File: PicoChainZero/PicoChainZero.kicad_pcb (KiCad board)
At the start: 2 copper layers, 60 x 60 mm, 16 parts, among them J1 RJ45, J2 RJ45, J4 +24V, J5 Conn_02x20_Odd_Even, J6 +12V, J7 USB_C_Receptacle_USB2.0_14P, U1 LM78M05, U2 PCA9615DP, U3 FT232RL

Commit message: Added open source hardware logo to PCBs
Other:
- board text added: "The TAPR Open Hardware License http://www.tapr.org/OHL"

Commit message: Regenerated gerbers
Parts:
- J4: value +24V -> Screw Terminal
- J6: value +12V -> Screw Terminal
- U1: value LM78M05 -> LM78M05_TO252
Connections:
- U3 pad 4: unconnected-(U3-VCCIO-Pad4) -> +5V
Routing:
- net +5V: track 57.9 -> 80.4 mm, vias 0 -> 2

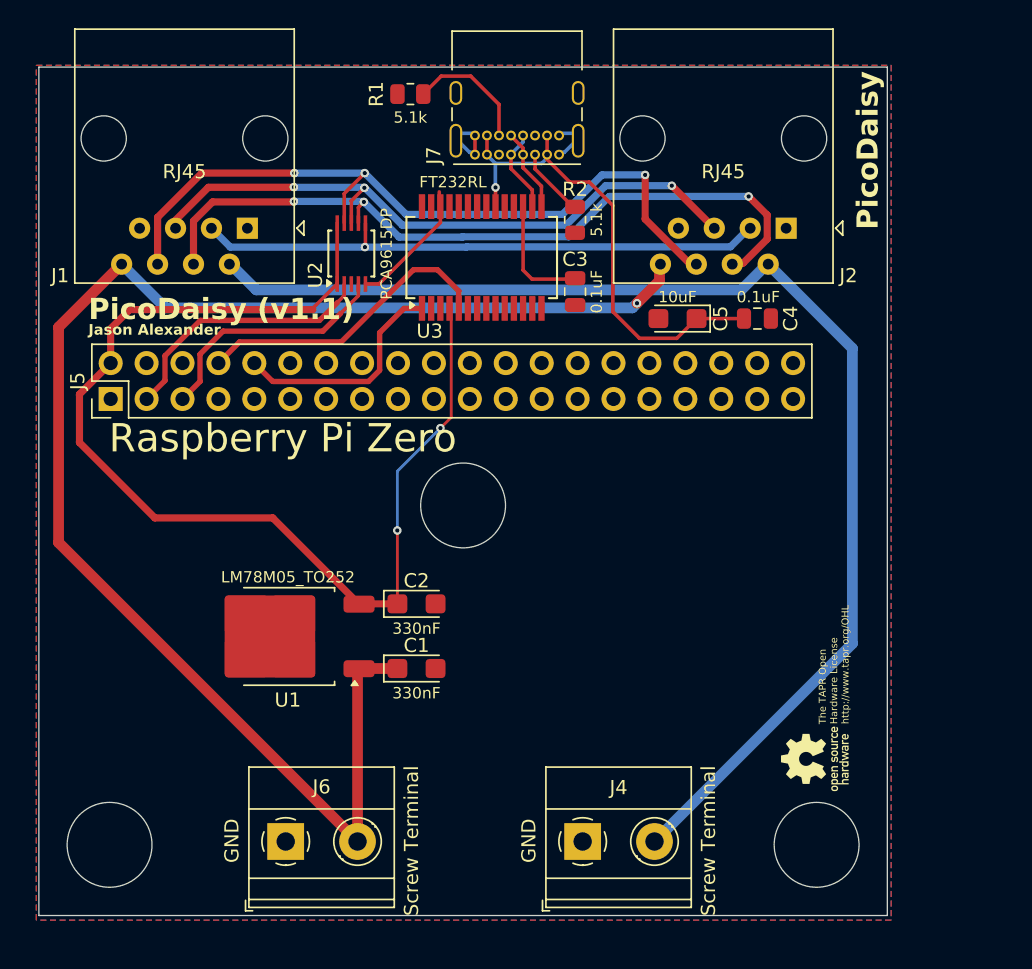
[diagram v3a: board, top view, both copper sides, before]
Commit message: Made pass through power rails larger.
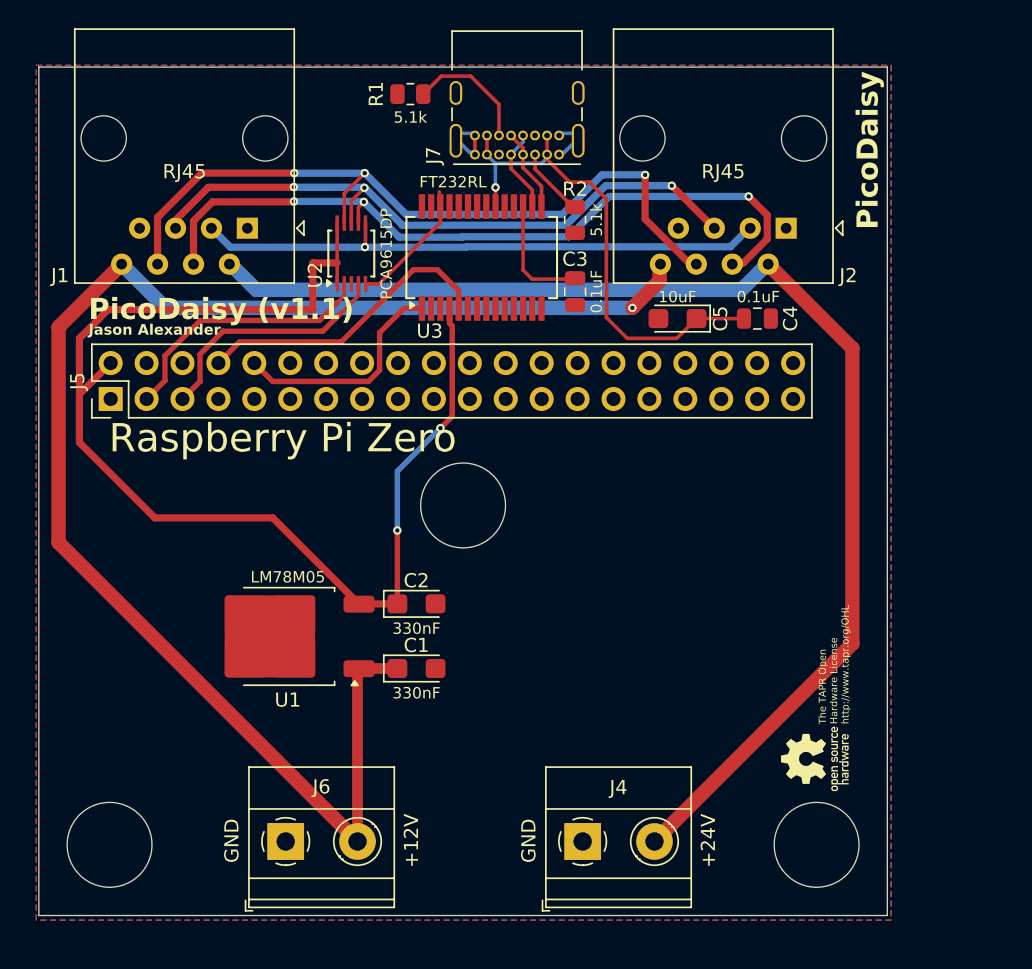
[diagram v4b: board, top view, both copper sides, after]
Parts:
- J4: value Screw Terminal -> +24V
- J6: value Screw Terminal -> +12V
- U1: value LM78M05_TO252 -> LM78M05
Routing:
- net +5V: track 80.4 -> 87.1 mm
- net Net-(U3-VCC): track 35.5 -> 36.0 mm
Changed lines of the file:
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@@
 			)
 		)
-		(property "Value" "Screw Terminal"
+		(property "Value" "+12V"
 			(at 8.895 -0.051 90)
 			(layer "F.SilkS")
@@
 			)
 		)
-		(property "Value" "Screw Terminal"
+		(property "Value" "+24V"
 			(at 8.895 -0.051 90)
 			(layer "F.SilkS")
@@
 		(tags "USB Type-C Receptacle Through-hole Right angle")
 		(property "Reference" "J7"
-			(at 8.865 -0.067 90)
+			(at 8.8746 -0.0644 90)
 			(layer "F.SilkS")
 			(effects
@@
 			)
 		)
-		(property "Value" "LM78M05_TO252"
+		(property "Value" "LM78M05"
 			(at -0.01 4.191 0)
 			(layer "F.SilkS")
@@
 	)
 	(segment
-		(start 105.077 58.499)
-		(end 105.077 60.932)
-		(width 0.508)
+		(start 125.353 72.775)
+		(end 125.353 77.959)
+		(width 0.381)
 		(layer "F.Cu")
 		(net 2)
 	)
 	(segment
-		(start 119.38 57.15)
-		(end 119.38 57.05)
-		(width 0.254)
+		(start 104.902 57.15)
+		(end 119.38 57.15)
+		(width 0.508)
 		(layer "F.Cu")
 		(net 2)
 	)
 	(segment
-		(start 129.159 64.77)
-		(end 128.397 65.532)
+		(start 129.043 57.067)
+		(end 129.159 57.183)
 		(width 0.2)
 		(layer "F.Cu")
@@
 	)
 	(segment
-		(start 125.353 72.775)
-		(end 125.353 77.959)
-		(width 0.2)
+		(start 121.095 53.848)
+		(end 121.095 51.035)
+		(width 0.254)
 		(layer "F.Cu")
 		(net 2)
 	)
 	(segment
-		(start 106.426 57.15)
-		(end 105.077 58.499)
+		(start 102.87 63.139)
+		(end 102.87 59.182)
 		(width 0.508)
 		(layer "F.Cu")
@@
 	)
 	(segment
-		(start 129.043 57.067)
-		(end 129.159 57.183)
-		(width 0.2)
+		(start 102.87 59.182)
+		(end 104.902 57.15)
+		(width 0.508)
+		(layer "F.Cu")
+		(net 2)
+	)
+	(segment
+		(start 129.2352 58.30522)
+		(end 129.043 58.11302)
+		(width 0.381)
 		(layer "F.Cu")
 		(net 2)
@@
 	)
 	(segment
+		(start 129.2352 64.6938)
+		(end 129.2352 58.30522)
+		(width 0.381)
+		(layer "F.Cu")
+		(net 2)
+	)
+	(segment
 		(start 119.38 57.15)
-		(end 106.426 57.15)
+		(end 119.38 53.848)
 		(width 0.508)
 		(layer "F.Cu")
@@
 	)
 	(segment
+		(start 121.095 55.335)
+		(end 121.095 53.848)
+		(width 0.254)
+		(layer "F.Cu")
+		(net 2)
+	)
+	(segment
 		(start 102.87 66.548)
 		(end 108.204 71.882)
@@
 	)
 	(segment
-		(start 129.159 57.183)
-		(end 129.159 64.77)
-		(width 0.2)
+		(start 105.077 60.932)
+		(end 102.87 63.139)
+		(width 0.508)
 		(layer "F.Cu")
 		(net 2)
 	)
 	(segment
-		(start 105.077 60.932)
-		(end 102.87 63.139)
-		(width 0.508)
+		(start 128.397 65.532)
+		(end 129.2352 64.6938)
+		(width 0.381)
 		(layer "F.Cu")
 		(net 2)
@@
 	)
 	(segment
-		(start 121.095 55.335)
-		(end 121.095 51.035)
-		(width 0.254)
+		(start 125.353 77.959)
+		(end 122.667 77.959)
+		(width 0.508)
 		(layer "F.Cu")
 		(net 2)
 	)
 	(segment
-		(start 125.353 77.959)
-		(end 122.667 77.959)
-		(width 0.508)
+		(start 129.043 58.11302)
+		(end 129.043 57.067)
+		(width 0.381)
 		(layer "F.Cu")
 		(net 2)
@@
 	)
 	(segment
-		(start 119.38 57.05)
-		(end 121.095 55.335)
-		(width 0.254)
+		(start 125.353 72.767)
+		(end 125.349 72.771)
+		(width 0.2)
 		(layer "F.Cu")
 		(net 2)
 	)
 	(segment
-		(start 125.353 72.767)
-		(end 125.349 72.771)
-		(width 0.2)
+		(start 119.38 53.848)
+		(end 121.095 53.848)
+		(width 0.508)
 		(layer "F.Cu")
 		(net 2)
@@
 		(start 128.397 65.532)
 		(end 125.353 68.576)
-		(width 0.2)
+		(width 0.381)
 		(layer "B.Cu")
 		(net 2)
@@
 		(start 125.353 68.576)
 		(end 125.353 72.767)
-		(width 0.2)
+		(width 0.381)
 		(layer "B.Cu")
 		(net 2)
@@
 		(start 105.8545 53.936)
 		(end 101.394 58.3965)
-		(width 0.762)
+		(width 1.016)
 		(layer "F.Cu")
 		(net 3)
 	)
 	(segment
-		(start 142.299 56.701)
-		(end 143.891 55.109)
+		(start 125.353 82.531)
+		(end 122.655 82.531)
 		(width 0.762)
 		(layer "F.Cu")
@@
 	)
 	(segment
-		(start 143.891 55.109)
-		(end 143.891 53.9995)
+		(start 122.535 82.651)
+		(end 122.642 82.544)
 		(width 0.762)
 		(layer "F.Cu")
@@
 	)
 	(segment
-		(start 125.353 82.531)
-		(end 122.655 82.531)
-		(width 0.762)
+		(start 143.891 55.109)
+		(end 143.891 53.9995)
+		(width 1.016)
 		(layer "F.Cu")
 		(net 3)
 	)
 	(segment
-		(start 122.535 82.651)
-		(end 122.642 82.544)
+		(start 143.891 53.9995)
+		(end 143.9545 53.936)
 		(width 0.762)
 		(layer "F.Cu")
@@
 	)
 	(segment
-		(start 143.891 53.9995)
-		(end 143.9545 53.936)
-		(width 0.762)
+		(start 141.973 57.027)
+		(end 143.891 55.109)
+		(width 1.016)
 		(layer "F.Cu")
 		(net 3)
@@
 		(start 101.394 73.624)
 		(end 122.535 94.765)
-		(width 0.762)
+		(width 1.016)
 		(layer "F.Cu")
 		(net 3)
@@
 		(start 101.394 58.3965)
 		(end 101.394 73.624)
-		(width 0.762)
+		(width 1.016)
 		(layer "F.Cu")
 		(net 3)
 	)
 	(via
-		(at 142.299 56.701)
+		(at 141.973 57.027)
 		(size 0.6)
 		(drill 0.3)
@@
 	)
 	(segment
-		(start 142.299 56.701)
-		(end 141.973 57.027)
-		(width 0.762)
-		(layer "B.Cu")
-		(net 3)
-	)
-	(segment
 		(start 108.9455 57.027)
 		(end 105.8545 53.936)
-		(width 0.762)
+		(width 1.016)
 		(layer "B.Cu")
 		(net 3)
@@
 		(start 141.973 57.027)
 		(end 108.9455 57.027)
-		(width 0.762)
+		(width 1.016)
 		(layer "B.Cu")
 		(net 3)
@@
 	)
 	(segment
-		(start 137.541 48.133)
-		(end 135.939 46.531)
+		(start 131.689 46.034)
+		(end 131.689 44.684)
 		(width 0.254)
 		(layer "F.Cu")
@@
 	)
 	(segment
-		(start 131.689 46.034)
-		(end 131.689 44.684)
+		(start 138.938 48.133)
+		(end 137.541 48.133)
 		(width 0.254)
 		(layer "F.Cu")
@@
 	)
 	(segment
-		(start 145.114 59.182)
-		(end 142.478 59.182)
+		(start 141.605 59.182)
+		(end 140.1318 57.7088)
 		(width 0.254)
 		(layer "F.Cu")
@@
 	)
 	(segment
-		(start 140.589 57.293)
-		(end 140.589 49.784)
+		(start 137.541 48.133)
+		(end 135.939 46.531)
 		(width 0.254)
 		(layer "F.Cu")
@@
 	)
 	(segment
-		(start 140.589 49.784)
-		(end 138.938 48.133)
+		(start 135.939 46.531)
+		(end 135.939 44.684)
 		(width 0.254)
 		(layer "F.Cu")
@@
 	)
 	(segment
-		(start 138.938 48.133)
-		(end 137.541 48.133)
+		(start 132.293 48.514)
+		(end 132.293 49.867)
 		(width 0.254)
 		(layer "F.Cu")
@@
 	)
 	(segment
-		(start 132.293 48.514)
-		(end 132.293 49.867)
+		(start 140.1318 49.3268)
+		(end 138.938 48.133)
 		(width 0.254)
 		(layer "F.Cu")
@@
 	)
 	(segment
-		(start 142.478 59.182)
-		(end 140.589 57.293)
+		(start 145.114 59.182)
+		(end 141.605 59.182)
 		(width 0.254)
 		(layer "F.Cu")
@@
 	)
 	(segment
-		(start 135.939 46.531)
-		(end 135.939 44.684)
+		(start 146.511 57.785)
+		(end 145.114 59.182)
 		(width 0.254)
 		(layer "F.Cu")
@@
 	)
 	(segment
-		(start 146.511 57.785)
-		(end 145.114 59.182)
+		(start 140.1318 57.7088)
+		(end 140.1318 49.3268)
 		(width 0.254)
 		(layer "F.Cu")
@@
 		(start 157.528 80.772)
 		(end 157.528 59.8895)
-		(width 0.762)
-		(layer "B.Cu")
+		(width 1.016)
+		(layer "F.Cu")
 		(net 11)
 	)
 	(segment
-		(start 113.4745 53.856)
-		(end 115.3755 55.757)
-		(width 0.762)
-		(layer "B.Cu")
+		(start 151.5745 53.936)
+		(end 157.528 59.8895)
+		(width 1.016)
+		(layer "F.Cu")
 		(net 11)
 	)
 	(segment
-		(start 115.3755 55.757)
-		(end 149.6735 55.757)
-		(width 0.762)
-		(layer "B.Cu")
+		(start 143.535 94.765)
+		(end 157.528 80.772)
+		(width 1.016)
+		(layer "F.Cu")
 		(net 11)
 	)
 	(segment
-		(start 151.5745 53.936)
-		(end 157.528 59.8895)
-		(width 0.762)
+		(start 113.4745 53.856)
+		(end 115.3755 55.757)
+		(width 1.016)
 		(layer "B.Cu")
 		(net 11)
 	)
 	(segment
-		(start 143.535 94.765)
-		(end 157.528 80.772)
-		(width 0.762)
+		(start 115.3755 55.757)
+		(end 149.6735 55.757)
+		(width 1.016)
 		(layer "B.Cu")
 		(net 11)
@@
 		(start 149.6735 55.757)
 		(end 151.5745 53.856)
-		(width 0.762)
+		(width 1.016)
 		(layer "B.Cu")
 		(net 11)

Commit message: Updated PicoChainZero base board.
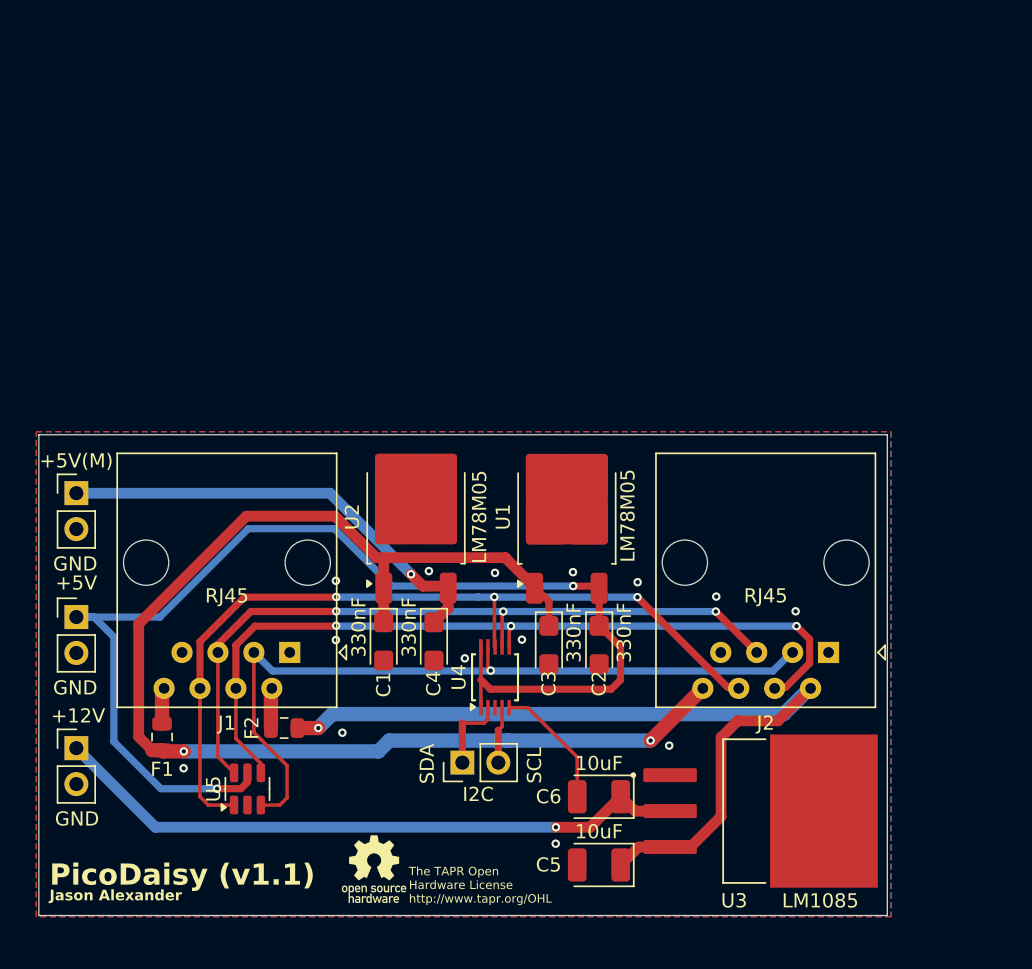
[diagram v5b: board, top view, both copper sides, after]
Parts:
- removed J7: USB_C_Receptacle_USB2.0_14P, Connector_USB:USB_C_Receptacle_GCT_USB4085
- removed R1, R2: 5.1k, Resistor_SMD:R_0805_2012Metric
- added C6: 10uF, Capacitor_Tantalum_SMD:CP_EIA-3528-21_Kemet-B, F.Cu at (139.6, 91.6)
- added F1: Fuse, Fuse:Fuse_0805_2012Metric, F.Cu at (108.7, 87.4)
- added F2: Fuse, Fuse:Fuse_0805_2012Metric, F.Cu at (117.3, 86.7)
- added J3: +12V, Connector_PinHeader_2.54mm:PinHeader_1x02_P2.54mm_Vertical, F.Cu at (102.7, 88.2)
- added U1: LM78M05, Package_TO_SOT_SMD:TO-252-2, F.Cu at (137.3, 71.8)
- added U5: SRV05, Package_TO_SOT_SMD:SOT-23-6, F.Cu at (114.8, 91.0)
- C3, C4: value 0.1uF -> 330nF; footprint Capacitor_SMD:C_0805_2012Metric -> Capacitor_Tantalum_SMD:CP_EIA-3216-18_Kemet-A
- C5: footprint Capacitor_Tantalum_SMD:CP_EIA-3216-18_Kemet-A -> Capacitor_Tantalum_SMD:CP_EIA-3528-21_Kemet-B
- J4: value +24V -> +5V(M); footprint TerminalBlock_Phoenix:TerminalBlock_Phoenix_MKDS-1,5-2-5.08_1x02_P5.08mm_Horizontal -> Connector_PinHeader_2.54mm:PinHeader_1x02_P2.54mm_Vertical
- J5: value Conn_02x20_Odd_Even -> I2C; footprint Connector_PinHeader_2.54mm:PinHeader_2x20_P2.54mm_Vertical -> Connector_PinHeader_2.54mm:PinHeader_1x02_P2.54mm_Vertical
- J6: value +12V -> +5V; footprint TerminalBlock_Phoenix:TerminalBlock_Phoenix_MKDS-1,5-2-5.08_1x02_P5.08mm_Horizontal -> Connector_PinHeader_2.54mm:PinHeader_1x02_P2.54mm_Vertical
- U3: value FT232RL -> LM1085; footprint Package_SO:SSOP-28_5.3x10.2mm_P0.65mm -> LM1085IS-12:TO254P1524X483-4N
- moved U3 43.8 mm to (151.0, 92.6), turned to 0 degrees
- moved J4 43.5 mm to (102.7, 70.1)
- moved C5 39.0 mm to (139.6, 96.4)
- moved J5 35.8 mm to (130.0, 89.2)
- moved C4 32.3 mm to (127.9, 80.6), turned to -90 degrees
- moved U4 31.6 mm to (132.3, 83.2)
- moved J1 30.1 mm to (117.7, 81.4)
- moved J2 30.1 mm to (155.8, 81.4)
- moved C3 25.1 mm to (136.1, 80.9), turned to -90 degrees
- moved J6 21.7 mm to (102.7, 78.9)
- moved C2 13.2 mm to (139.6, 80.9), turned to -90 degrees
- moved U2 12.4 mm to (126.7, 71.8), turned to 90 degrees
- moved C1 3.01 mm to (124.4, 80.6), turned to -90 degrees
- renumbered U1 to U2, U2 to U4
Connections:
- C3 pad 1: GND -> +12V
- C3 pad 2: Net-(U3-3V3OUT) -> GND
- C4 pad 1: Net-(U3-VCC) -> /+5V(M)
- C5 pad 1: Net-(U3-VCC) -> +24V
- J1 pad 2: +24V -> Net-(F2-Pad1)
- J1 pad 3: Net-(U2-DSCLM) -> Net-(U4-DSDAM)
- J1 pad 4: Net-(U2-DSCLP) -> Net-(U4-DSCLM)
- J1 pad 5: Net-(U2-DSDAP) -> Net-(U4-DSCLP)
- J1 pad 6: Net-(U2-DSDAM) -> Net-(U4-DSDAP)
- J1 pad 8: +12V -> Net-(F1-Pad1)
- J2 pad 3: Net-(U2-DSCLM) -> Net-(U4-DSDAM)
- J2 pad 4: Net-(U2-DSCLP) -> Net-(U4-DSCLM)
- J2 pad 5: Net-(U2-DSDAP) -> Net-(U4-DSCLP)
- J2 pad 6: Net-(U2-DSDAM) -> Net-(U4-DSDAP)
- J4 pad 1: GND -> /+5V(M)
- J4 pad 2: +24V -> GND
- J5 pad 1: unconnected-(J5-Pin_1-Pad1) -> Net-(J5-Pin_1)
- J5 pad 2: +5V -> Net-(J5-Pin_2)
- J6 pad 1: GND -> +5V
- J6 pad 2: +12V -> GND
- U2 pad 3: +5V -> /+5V(M)
- U3 pad 1: Net-(J5-Pin_10) -> GND
- U3 pad 2: unconnected-(U3-DTR-Pad2) -> /+12V(R)
- U3 pad 3: unconnected-(U3-RTS-Pad3) -> +24V
- U3 pad 4: +5V -> (no net)
- U4 pad 2: Net-(J5-Pin_3) -> Net-(J5-Pin_1)
- U4 pad 4: Net-(J5-Pin_5) -> Net-(J5-Pin_2)
- U4 pad 6: Net-(U2-DSCLM) -> Net-(U4-DSCLM)
- U4 pad 7: Net-(U2-DSCLP) -> Net-(U4-DSCLP)
- U4 pad 8: Net-(U2-DSDAP) -> Net-(U4-DSDAP)
- U4 pad 9: Net-(U2-DSDAM) -> Net-(U4-DSDAM)
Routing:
- net Net-(U4-DSDAP): track 0.00 -> 59.6 mm, vias 0 -> 3
- net Net-(U4-DSCLM): track 0.00 -> 57.2 mm, vias 0 -> 3
- net Net-(U4-DSDAM): track 0.00 -> 54.6 mm, vias 0 -> 1
- net Net-(U2-DSDAM): track 54.1 -> 0.00 mm, vias 3 -> 0
- net Net-(U2-DSCLP): track 53.0 -> 0.00 mm, vias 3 -> 0
- net Net-(U4-DSCLP): track 0.00 -> 52.3 mm, vias 0 -> 3
- net Net-(U2-DSDAP): track 46.0 -> 0.00 mm, vias 3 -> 0
- net /+12V(R): track 0.00 -> 45.6 mm, vias 0 -> 1
- net Net-(U2-DSCLM): track 41.0 -> 0.00 mm, vias 1 -> 0
- net Net-(U3-VCC): track 36.0 -> 0.00 mm, vias 1 -> 0
- net /+5V(M): track 0.00 -> 31.9 mm, vias 0 -> 1
- net +24V: track 88.8 -> 59.4 mm, vias 0 -> 1
- net Net-(J5-Pin_8): track 21.6 -> 0.00 mm
- net Net-(J5-Pin_3): track 18.9 -> 0.00 mm
- net Net-(J5-Pin_5): track 17.4 -> 0.00 mm
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- added copper zone on In1.Cu, net GND
- added copper zone on In2.Cu, net GND
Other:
- board size 60 x 60 mm -> 60 x 34 mm
- copper layers 2 -> 4
- board text added: "GND"
- board text added: "SCL"
- board text added: "SDA"
- board text removed: "PicoDaisy"
- board text removed: "Raspberry Pi Zero"
